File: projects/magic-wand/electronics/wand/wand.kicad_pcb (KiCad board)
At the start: 4 copper layers, 15 x 80 mm, 46 parts, among them J1 USB-C-16P, J2 SM03B-SRSS-TB, J3 SM02B-SRSS-TB, SW1 PRESS_TO_ARM, U1 NINA-B302-00B-00, U2 LSM6DSV16XTR, U3 BQ25185DLHR, U4 TPS63900DSKR, U5 DRV2605LDGSR, U6 USBLC6-2SC6

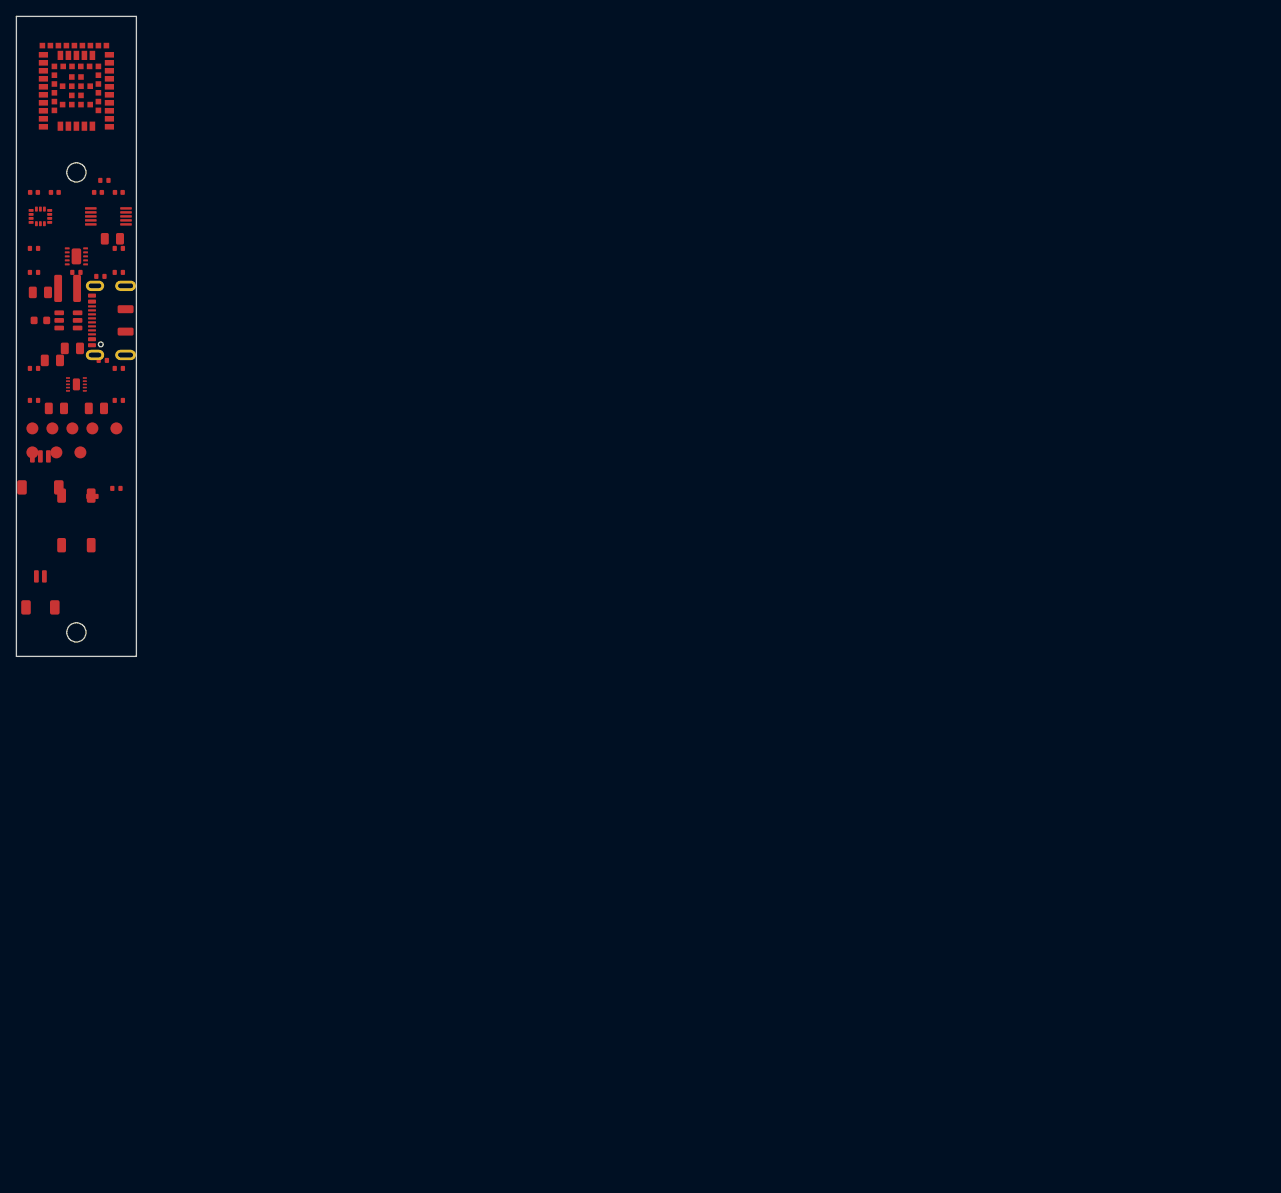
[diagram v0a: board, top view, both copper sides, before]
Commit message: fix: center generated KiCad boards on A4 worksheet
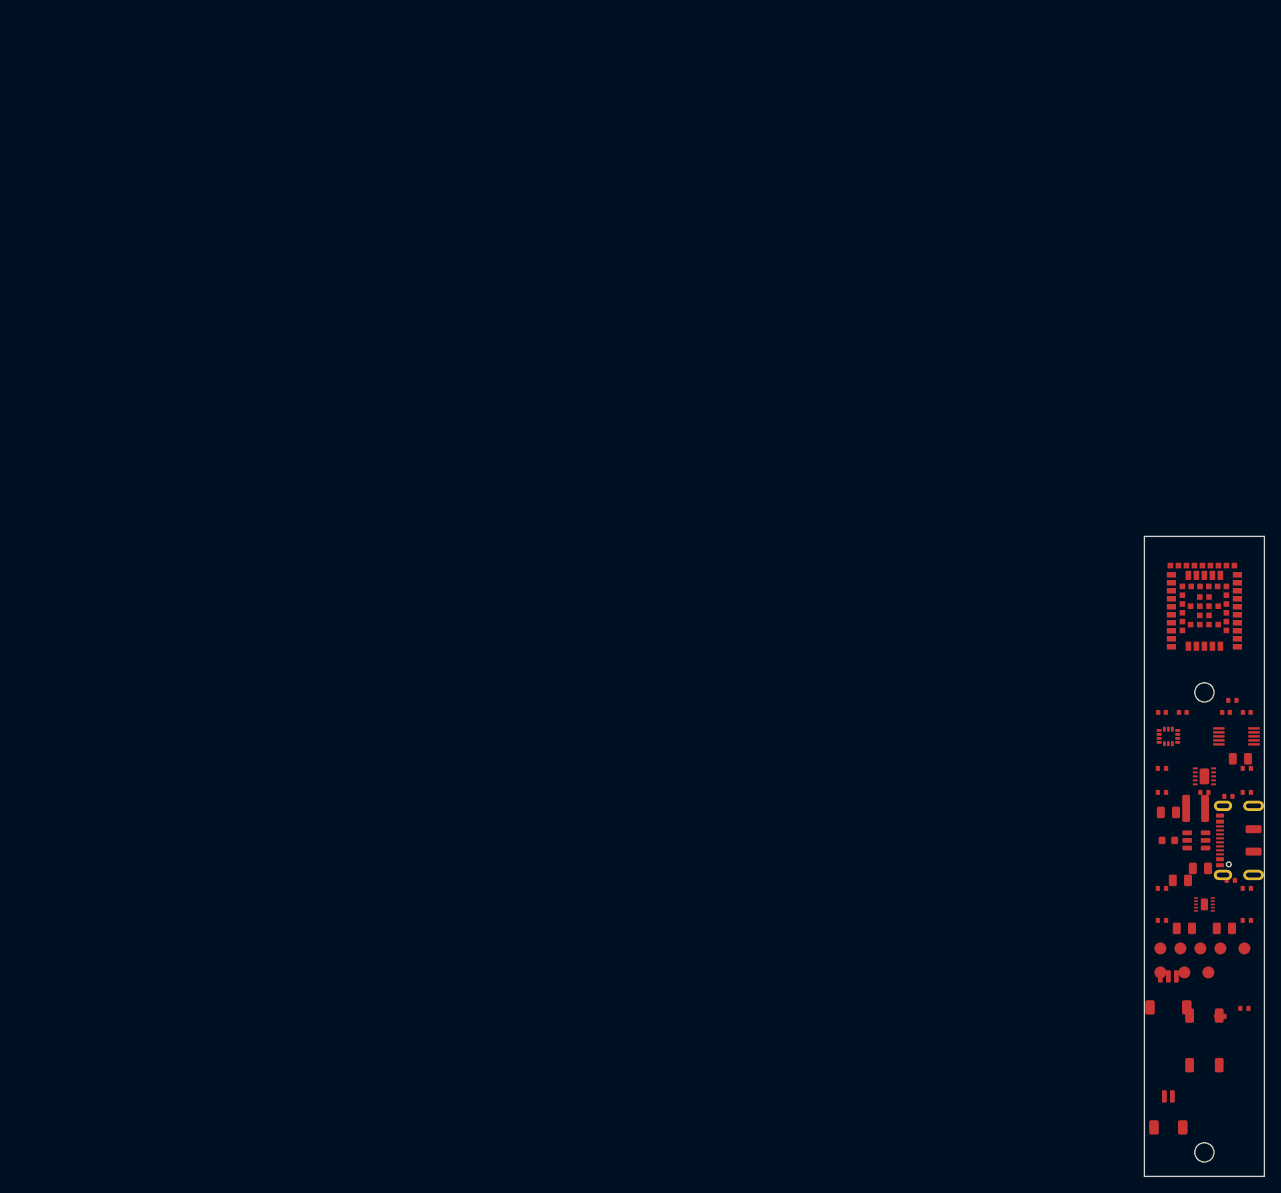
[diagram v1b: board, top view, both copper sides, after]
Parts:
- moved C_BAT 155.3 mm to (151.0, 114.0)
- moved C_BUCK_IN 155.3 mm to (144.0, 99.5)
- moved C_BUCK_OUT 155.3 mm to (153.0, 92.8)
- moved C_CHG_IN 155.3 mm to (145.5, 108.0)
- moved C_HAPTIC_REG 155.3 mm to (151.2, 87.0)
- moved C_HAPTIC_VDD 155.3 mm to (153.8, 87.0)
- moved C_IMU_IO 155.3 mm to (145.8, 87.0)
- moved C_IMU_VDD 155.3 mm to (143.2, 87.0)
- moved C_SYS 155.3 mm to (146.0, 114.0)
- moved C_USB 155.3 mm to (148.0, 106.5)
- moved F1 155.3 mm to (144.0, 103.0)
- moved H1 155.3 mm to (148.5, 84.5)
- moved H2 155.3 mm to (148.5, 142.0)
- moved J1 155.3 mm to (153.5, 103.0)
- moved J2 155.3 mm to (144.0, 122.0)
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
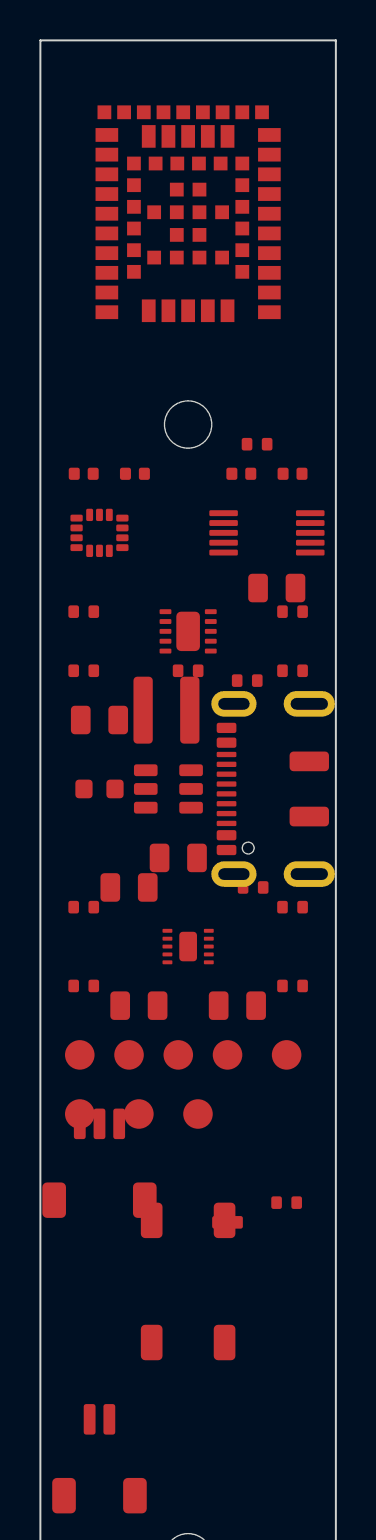
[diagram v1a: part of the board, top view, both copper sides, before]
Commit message: feat(magic-wand): freeze zero-error production routing
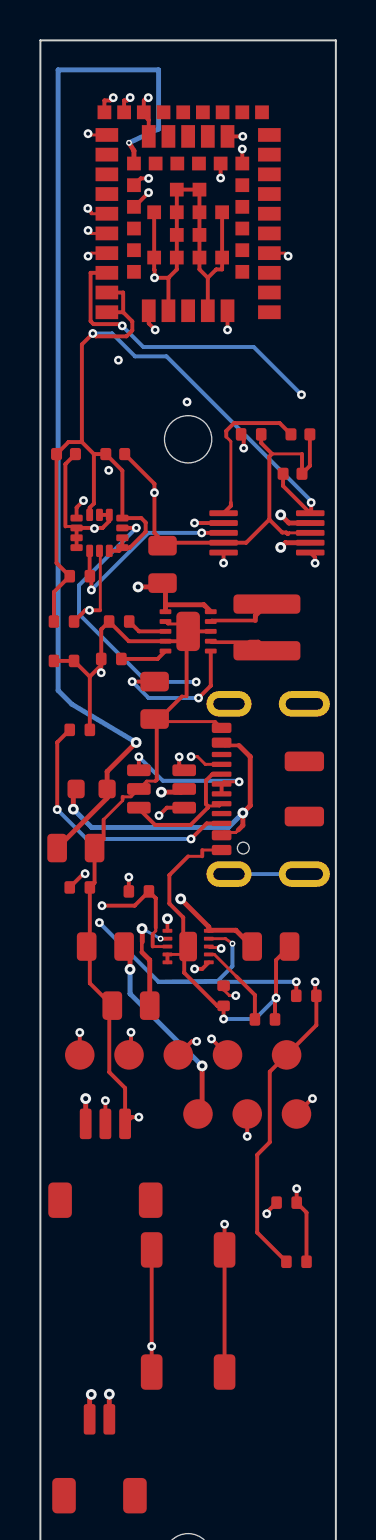
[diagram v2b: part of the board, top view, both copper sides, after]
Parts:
- moved R_STAT1 12.2 mm to (154.5, 113.5), turned to 180 degrees
- moved TP2 11.0 mm to (154.0, 119.5)
- moved R_I2C_SDA 10.9 mm to (143.0, 92.2)
- moved R_CFG3 9.22 mm to (144.6, 96.4), turned to 180 degrees
- moved R_CC1 8.86 mm to (143.0, 100.0)
- moved R_CC2 8.80 mm to (143.0, 108.0)
- moved C_BUCK_IN 8.52 mm to (147.2, 91.6), turned to 90 degrees
- moved C_BUCK_OUT 8.42 mm to (146.8, 98.5), turned to 270 degrees
- moved R_STAT2 7.84 mm to (146.0, 108.2)
- moved C_CHG_IN 7.80 mm to (152.7, 111.0)
- moved R_ISET 7.12 mm to (150.3, 113.5), turned to 270 degrees
- moved L1 6.61 mm to (152.5, 94.8), turned to 270 degrees
- moved R_CFG2 6.32 mm to (142.2, 96.5)
- moved TP7 5.50 mm to (151.5, 119.5)
- moved C_BAT 5.40 mm to (145.6, 114.0), turned to 180 degrees
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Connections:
- U1 pad 1: (no net) -> HAPTIC_EN
- U1 pad 44: HAPTIC_EN -> (no net)
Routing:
- net GND: track 0.00 -> 194.5 mm, vias 0 -> 12
- net 3V3: track 0.00 -> 117.4 mm, vias 0 -> 7
- net USB_VBUS_5V: track 0.00 -> 75.7 mm, vias 0 -> 4
- net ARM_N: track 0.00 -> 57.6 mm, vias 0 -> 2
- net CHG_STAT1_N: track 0.00 -> 57.2 mm, vias 0 -> 4
- net HAPTIC_N: track 0.00 -> 55.0 mm, vias 0 -> 2
- net SWO: track 0.00 -> 53.2 mm, vias 0 -> 3
- net HAPTIC_P: track 0.00 -> 51.0 mm, vias 0 -> 2
- net RESET_N: track 0.00 -> 46.1 mm, vias 0 -> 2
- net CHG_STAT2_N: track 0.00 -> 41.3 mm, vias 0 -> 2
- net SWDIO: track 0.00 -> 41.1 mm, vias 0 -> 3
- net USB_DM_PROT: track 0.00 -> 40.2 mm, vias 0 -> 2
- net TP_IMU_INT2: track 0.00 -> 39.8 mm, vias 0 -> 3
- net SWDCLK: track 0.00 -> 39.3 mm, vias 0 -> 3
- net I2C_SCL: track 0.00 -> 38.8 mm, vias 0 -> 3
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
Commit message: feat(magic-wand): complete wand BOM LCSC 36/36 and rebuild JLC package
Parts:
- C_HAPTIC_REG, C_HAPTIC_VDD: value 1uF 10V X7R -> 1uF 10V X5R
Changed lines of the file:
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@@
     (at 154.2000 85.0000 0.0)
     (property "Reference" "C_HAPTIC_REG" (at 0 -1.250 0.0) (layer "F.Fab") (effects (font (size 0.80 0.80)) hide))
-    (property "Value" "1uF 10V X7R" (at 0 1.250 0.0) (layer "F.Fab") (effects (font (size 0.70 0.70))))
-    (property "Manufacturer" "Murata" (at 0 0 0.0) (layer "F.Fab") (effects (font (size 0.60 0.60)) hide))
-    (property "MPN" "GRM155R71A105KE15D" (at 0 0 0.0) (layer "F.Fab") (effects (font (size 0.60 0.60)) hide))
+    (property "Value" "1uF 10V X5R" (at 0 1.250 0.0) (layer "F.Fab") (effects (font (size 0.70 0.70))))
+    (property "Manufacturer" "Samsung Electro-Mechanics" (at 0 0 0.0) (layer "F.Fab") (effects (font (size 0.60 0.60)) hide))
+    (property "MPN" "CL05A105KP5NNNC" (at 0 0 0.0) (layer "F.Fab") (effects (font (size 0.60 0.60)) hide))
     (attr smd)
     (fp_rect (start -0.500 -0.250) (end 0.500 0.250) (stroke (width 0.10) (type solid)) (fill none) (layer "F.Fab"))
@@
     (at 153.8000 87.0000 0.0)
     (property "Reference" "C_HAPTIC_VDD" (at 0 -1.250 0.0) (layer "F.Fab") (effects (font (size 0.80 0.80)) hide))
-    (property "Value" "1uF 10V X7R" (at 0 1.250 0.0) (layer "F.Fab") (effects (font (size 0.70 0.70))))
-    (property "Manufacturer" "Murata" (at 0 0 0.0) (layer "F.Fab") (effects (font (size 0.60 0.60)) hide))
-    (property "MPN" "GRM155R71A105KE15D" (at 0 0 0.0) (layer "F.Fab") (effects (font (size 0.60 0.60)) hide))
+    (property "Value" "1uF 10V X5R" (at 0 1.250 0.0) (layer "F.Fab") (effects (font (size 0.70 0.70))))
+    (property "Manufacturer" "Samsung Electro-Mechanics" (at 0 0 0.0) (layer "F.Fab") (effects (font (size 0.60 0.60)) hide))
+    (property "MPN" "CL05A105KP5NNNC" (at 0 0 0.0) (layer "F.Fab") (effects (font (size 0.60 0.60)) hide))
     (attr smd)
     (fp_rect (start -0.500 -0.250) (end 0.500 0.250) (stroke (width 0.10) (type solid)) (fill none) (layer "F.Fab"))
